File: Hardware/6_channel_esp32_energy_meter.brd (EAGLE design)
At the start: 61 x 62.2 mm, 117 parts, among them IC1 ATM90E32AS, IC2 ATM90E32AS, IC3 LMR14020SDDA, J16 PINHD-1X19, J4 9-12VAC, J5 PINHD1X1-SM1X01_SM, J6 PINHD1X1-SM1X01_SM, J8 PINHD1X1-SM1X01_SM, U1 ESP32-DEVKITC-32D, Y1 16.384MHz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

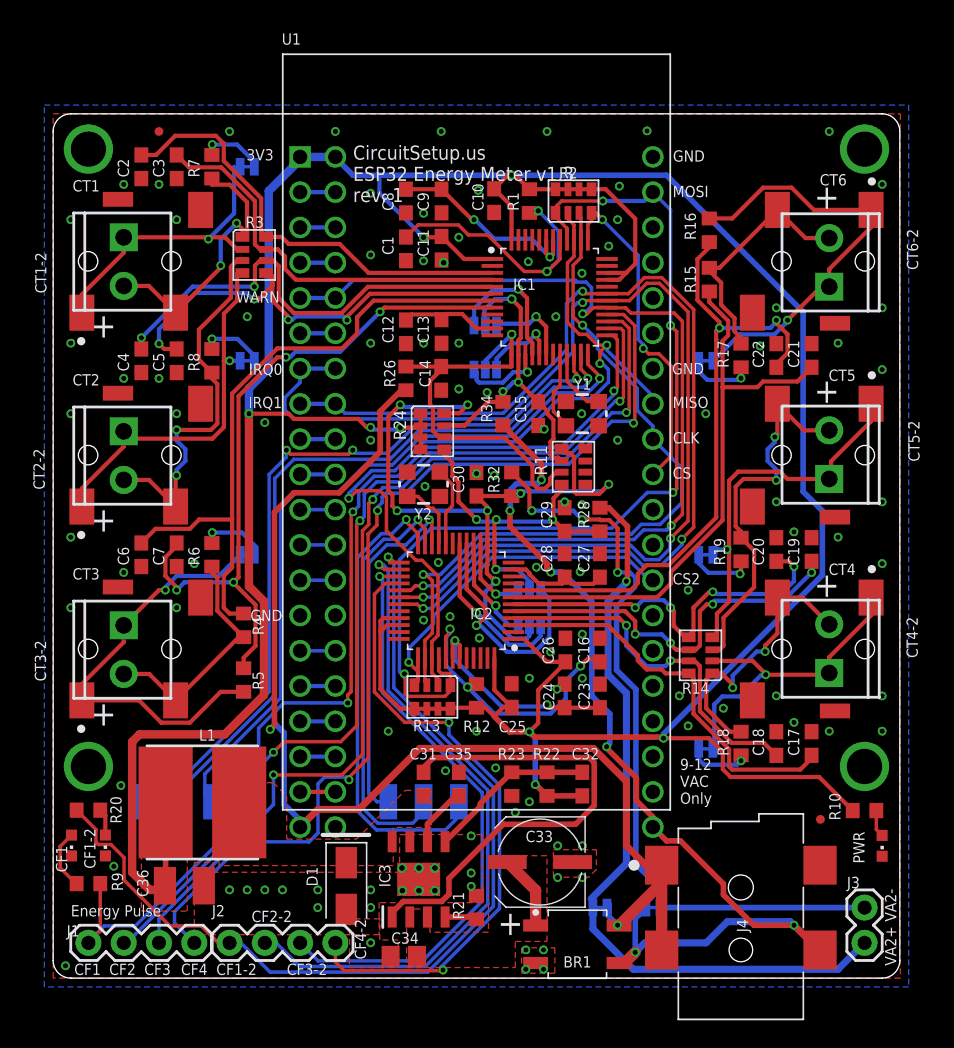
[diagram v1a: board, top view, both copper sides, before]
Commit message: v1.4
- Added optional micro-hdmi connection to connect the current transformer remote board. This allows for all 6 current transformer connections to connect to a remote pcb, which then connects to the main board via 1 micro-hdmi cable. Instead of 6 wires coming out of the meter, there can now be 1.
- Added current transformer remote pcb
- Removed JP8-JP11 and connected all voltage channels together for each ATM90E32
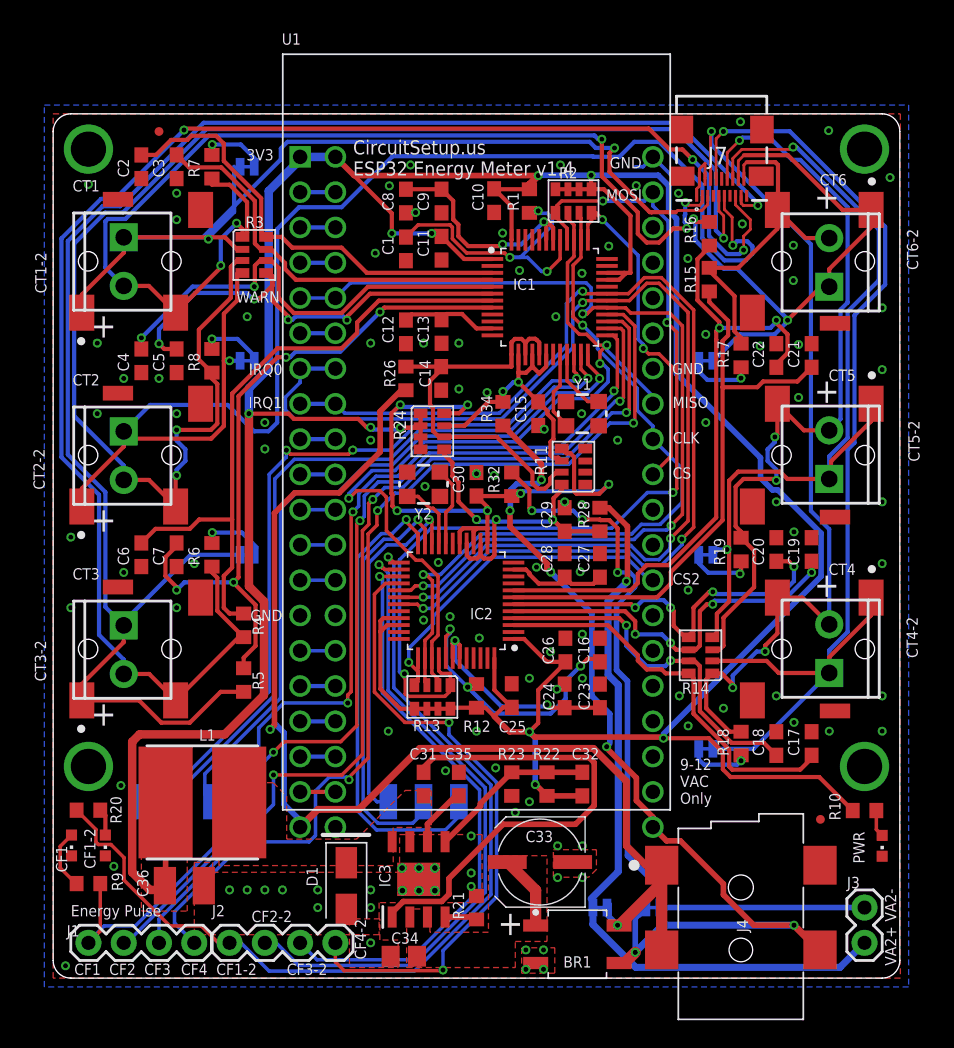
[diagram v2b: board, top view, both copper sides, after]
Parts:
- removed JP10, JP11, JP8, JP9: JUMPER-SMT_3_NO_SILK, SparkFun-Jumpers:SMT-JUMPER_3_NO_SILK
- added J7: 46765-0001, 46765-0001:46765-0001
- moved R16 0.25 mm to (47.2, 53.6)
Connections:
- removed net V2N: IC1.16, JP9.3
- removed net V2N-2: IC2.16, JP11.3
- removed net V2P: IC1.15, JP8.3
- removed net V2P-2: IC2.15, JP10.3
- removed net V3N: IC1.18, JP9.1
- removed net V3N-2: IC2.18, JP11.1
- removed net V3P: IC1.17, JP8.1
- removed net V3P-2: IC2.17, JP10.1
- net GND: now also J7.1, J7.10, J7.13, J7.2, J7.4, J7.7
- net IA+: now also J7.3
- net IA+-2: now also J7.6
- net IA-: now also J7.5
- net IA--2: now also J7.8
- net IB+: now also J7.9
- net IB+-2: now also J7.12
- net IB-: now also J7.11
- net IB--2: now also J7.14
- net IC+: now also J7.15
- net IC+-2: now also J7.18
- net IC-: now also J7.17
- net IC--2: now also J7.16
- net VAN: now also IC1.16, IC1.18; no longer JP9.2
- net VAN2: now also IC2.16, IC2.18; no longer JP11.2
- net VAP: now also IC1.15, IC1.17; no longer JP8.2
- net VAP2: now also IC2.15, IC2.17; no longer JP10.2
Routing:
- net IC+: track 17.3 -> 113.9 mm, vias 0 -> 3
- net IC-: track 30.5 -> 117.4 mm
- net IB+: track 27.5 -> 105.2 mm, vias 2 -> 3
- net IB-: track 27.6 -> 103.2 mm, vias 1 -> 2
- net IA+: track 20.1 -> 79.6 mm, vias 2 -> 5
- net IA--2: track 23.4 -> 78.0 mm
- net IA-: track 22.0 -> 71.8 mm, vias 1 -> 2
- net IA+-2: track 20.7 -> 63.1 mm, vias 2 -> 3
- net IB--2: track 27.5 -> 61.8 mm, vias 1 -> 2
- net IB+-2: track 27.7 -> 57.3 mm, vias 2 -> 3
- net V3P-2: track 17.0 -> 0.00 mm, vias 1 -> 0
- net V3N-2: track 12.1 -> 0.00 mm, vias 1 -> 0
- net IC--2: track 30.7 -> 41.4 mm, vias 1 -> 2
- net V2N: track 10.3 -> 0.00 mm, vias 1 -> 0
- net IC+-2: track 17.6 -> 25.3 mm
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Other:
- board text added: "CircuitSetup.us ESP32 Energy Meter v1.4"
- board text removed: "CircuitSetup.us ESP32 Energy Meter v1.3 rev. 1"
- board text removed: "JP8 - JP11: Connect the center pad with the 2 outer pads to connect all 3 voltage channels together for each IC"

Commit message: v1.4 rev1
- Changed micro-hdmi connector to through-hole
- Changed spacing on VA2+/VA2- (voltage 2 connection) to 3.5mm to allow for standard screw connectors
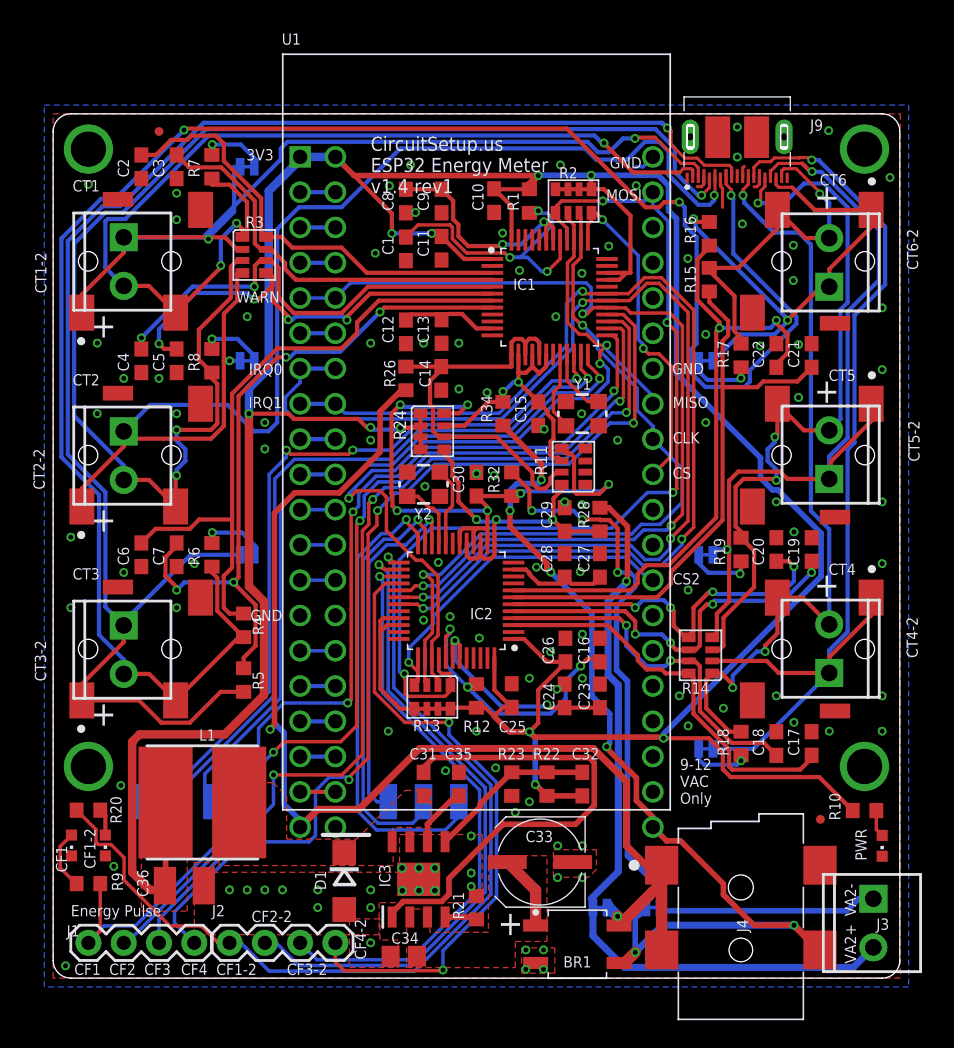
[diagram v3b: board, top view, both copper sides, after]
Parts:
- removed J7: 46765-0001, 46765-0001:46765-0001
- added J9: PKS019-4011-0, SamacSys_Parts:PKS01940110
- D1: value 500mV 3A -> (none); device SamacSys_Parts:DIOM4326X240 -> diode:DO214AC
- J3: device SparkFun-Connectors:1X02 -> SparkFun-Connectors:SCREWTERMINAL-3.5MM-2
- moved J3 3.24 mm to (59.1, 5.71), turned to 270 degrees
- moved D1 0.39 mm to (21.0, 6.99)
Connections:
- net GND: now also D1.A, J9.1, J9.10, J9.11, J9.14, J9.19, J9.21, J9.22, J9.4, J9.7, J9.P$1, J9.P$2; no longer D1.2, J7.1, J7.10, J7.13, J7.2, J7.4, J7.7
- net IA+: now also J9.2; no longer J7.3
- net IA+-2: now also J9.12; no longer J7.6
- net IA-: now also J9.3; no longer J7.5
- net IA--2: now also J9.13; no longer J7.8
- net IB+: now also J9.5; no longer J7.9
- net IB+-2: now also J9.15; no longer J7.12
- net IB-: now also J9.6; no longer J7.11
- net IB--2: now also J9.16; no longer J7.14
- net IC+: now also J9.8; no longer J7.15
- net IC+-2: now also J9.18; no longer J7.18
- net IC-: now also J9.9; no longer J7.17
- net IC--2: now also J9.17; no longer J7.16
- net SW: now also D1.C; no longer D1.1
- net VA2+: now also J3.2; no longer J3.1
- net VA2-: now also J3.1; no longer J3.2
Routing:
- net IC+: track 113.9 -> 137.4 mm
- net IB-: track 103.2 -> 93.9 mm
- net IA+: track 79.6 -> 71.8 mm, vias 5 -> 3
- net IA+-2: track 63.1 -> 56.6 mm
- net IB+: track 105.2 -> 99.1 mm
- net IA--2: track 78.0 -> 72.5 mm
- net IC--2: track 41.4 -> 36.1 mm
- net IB--2: track 61.8 -> 57.3 mm
- net IC-: track 117.4 -> 113.8 mm
- net IB+-2: track 57.3 -> 54.0 mm
- net IA-: track 71.8 -> 69.0 mm
- net VA+: track 88.7 -> 87.3 mm
- net VA2-: track 55.0 -> 56.1 mm
- net VA2+: track 54.0 -> 55.0 mm
- net IC+-2: track 25.3 -> 26.3 mm, vias 0 -> 1
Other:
- board text added: "CircuitSetup.us ESP32 Energy Meter v1.4 rev1"
- board text removed: "CircuitSetup.us ESP32 Energy Meter v1.4"

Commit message: Updated Eagle files to v1.4 rev1
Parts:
- C17, C18, C19, C2, C20, C21, C22, C3, C4, C5, C6, C7: value .33uF -> 18nf
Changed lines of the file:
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@@
 <?xml version="1.0" encoding="utf-8"?>
 <!DOCTYPE eagle SYSTEM "eagle.dtd">
-<eagle version="9.5.1">
+<eagle version="9.6.2">
 <drawing>
 <settings>
-<setting alwaysvectorfont="no"/>
+<setting alwaysvectorfont="yes"/>
 <setting keepoldvectorfont="yes"/>
 <setting verticaltext="up"/>
@@
 </layers>
 <board>
-<fusionsync huburn="a.cGVyc29uYWw6dWUyZGE1YzFh" projecturn="a.cGVyc29uYWw6dWUyZGE1YzFhIzIwMTgwODA3MTQyOTEzNDU2" f3durn="urn:adsk.wipprod:dm.lineage:77R0Z7BuTCq7n9YzdNgQcA" pcbguid="81154c38-d356-4f7c-b7d5-5c7aff837905" lastpulledtime="" lastsyncedchangeguid="6a4b892a-f070-e276-d825-ffa7404d0cf4"/>
+<fusionsync huburn="a.cGVyc29uYWw6dWUyZGE1YzFh" projecturn="a.cGVyc29uYWw6dWUyZGE1YzFhIzIwMTgwODA3MTQyOTEzNDU2" f3durn="urn:adsk.wipprod:dm.lineage:77R0Z7BuTCq7n9YzdNgQcA" pcbguid="81154c38-d356-4f7c-b7d5-5c7aff837905" lastpulledtime="" lastsyncedchangeguid="6a4b892a-f070-e276-d825-ffa7404d0cf4" latestrevisionid="" lastsyncedrevisionid="" lastboardhashguid="" lastpushedtime="" linktopcb3d="false"/>
 <plain>
 <text x="22.86" y="56.515" size="1.016" layer="25" font="vector" ratio="15">CircuitSetup.us
@@
 </autorouter>
 <elements>
-<element name="C2" library="rcl" library_urn="urn:adsk.eagle:library:334" package="C0603" package3d_urn="urn:adsk.eagle:package:23616/2" value=".33uF" x="6.35" y="58.42" smashed="yes" rot="R270">
+<element name="C2" library="rcl" library_urn="urn:adsk.eagle:library:334" package="C0603" package3d_urn="urn:adsk.eagle:package:23616/2" value="18nf" x="6.35" y="58.42" smashed="yes" rot="R270">
 <attribute name="NAME" x="5.461" y="57.658" size="0.8128" layer="25" font="vector" ratio="10" rot="R90"/>
 <attribute name="POPULARITY" value="37" x="6.35" y="58.42" size="1.778" layer="27" rot="R270" display="off"/>
@@
 <attribute name="VALUE" x="4.318" y="59.309" size="0.8" layer="27" rot="R270"/>
 </element>
-<element name="C3" library="rcl" library_urn="urn:adsk.eagle:library:334" package="C0603" package3d_urn="urn:adsk.eagle:package:23616/2" value=".33uF" x="8.89" y="58.42" smashed="yes" rot="R90">
+<element name="C3" library="rcl" library_urn="urn:adsk.eagle:library:334" package="C0603" package3d_urn="urn:adsk.eagle:package:23616/2" value="18nf" x="8.89" y="58.42" smashed="yes" rot="R90">
 <attribute name="NAME" x="8.001" y="57.658" size="0.8128" layer="25" font="vector" ratio="10" rot="R90"/>
 <attribute name="POPULARITY" value="37" x="8.89" y="58.42" size="1.778" layer="27" rot="R90" display="off"/>
@@
 <attribute name="VALUE" x="10.922" y="57.531" size="0.8" layer="27" rot="R90"/>
 </element>
-<element name="C4" library="rcl" library_urn="urn:adsk.eagle:library:334" package="C0603" package3d_urn="urn:adsk.eagle:package:23616/2" value=".33uF" x="6.35" y="44.45" smashed="yes" rot="R270">
+<element name="C4" library="rcl" library_urn="urn:adsk.eagle:library:334" package="C0603" package3d_urn="urn:adsk.eagle:package:23616/2" value="18nf" x="6.35" y="44.45" smashed="yes" rot="R270">
 <attribute name="NAME" x="5.461" y="43.688" size="0.8128" layer="25" font="vector" ratio="10" rot="R90"/>
 <attribute name="POPULARITY" value="37" x="6.35" y="44.45" size="1.778" layer="27" rot="R270" display="off"/>
@@
 <attribute name="VALUE" x="4.318" y="45.339" size="0.8" layer="27" rot="R270"/>
 </element>
-<element name="C5" library="rcl" library_urn="urn:adsk.eagle:library:334" package="C0603" package3d_urn="urn:adsk.eagle:package:23616/2" value=".33uF" x="8.89" y="44.45" smashed="yes" rot="R90">
+<element name="C5" library="rcl" library_urn="urn:adsk.eagle:library:334" package="C0603" package3d_urn="urn:adsk.eagle:package:23616/2" value="18nf" x="8.89" y="44.45" smashed="yes" rot="R90">
 <attribute name="NAME" x="8.001" y="43.688" size="0.8128" layer="25" font="vector" ratio="10" rot="R90"/>
 <attribute name="POPULARITY" value="37" x="8.89" y="44.45" size="1.778" layer="27" rot="R90" display="off"/>
@@
 <attribute name="VALUE" x="9.525" y="31.115" size="1.27" layer="27" rot="R270"/>
 </element>
-<element name="C6" library="rcl" library_urn="urn:adsk.eagle:library:334" package="C0603" package3d_urn="urn:adsk.eagle:package:23616/2" value=".33uF" x="6.35" y="30.48" smashed="yes" rot="R270">
+<element name="C6" library="rcl" library_urn="urn:adsk.eagle:library:334" package="C0603" package3d_urn="urn:adsk.eagle:package:23616/2" value="18nf" x="6.35" y="30.48" smashed="yes" rot="R270">
 <attribute name="NAME" x="5.461" y="29.718" size="0.8128" layer="25" font="vector" ratio="10" rot="R90"/>
 <attribute name="POPULARITY" value="37" x="6.35" y="30.48" size="1.778" layer="27" rot="R270" display="off"/>
@@
 <attribute name="VALUE" x="4.445" y="31.115" size="1.27" layer="27" rot="R270"/>
 </element>
-<element name="C7" library="rcl" library_urn="urn:adsk.eagle:library:334" package="C0603" package3d_urn="urn:adsk.eagle:package:23616/2" value=".33uF" x="8.89" y="30.48" smashed="yes" rot="R90">
+<element name="C7" library="rcl" library_urn="urn:adsk.eagle:library:334" package="C0603" package3d_urn="urn:adsk.eagle:package:23616/2" value="18nf" x="8.89" y="30.48" smashed="yes" rot="R90">
 <attribute name="NAME" x="8.001" y="29.718" size="0.8128" layer="25" font="vector" ratio="10" rot="R90"/>
 <attribute name="POPULARITY" value="37" x="8.89" y="30.48" size="1.778" layer="27" rot="R90" display="off"/>
@@
 <attribute name="VALUE" x="6.35" y="12.7" size="0.0254" layer="28" rot="MR0"/>
 </element>
-<element name="C17" library="rcl" library_urn="urn:adsk.eagle:library:334" package="C0603" package3d_urn="urn:adsk.eagle:package:23616/2" value=".33uF" x="54.61" y="16.891" smashed="yes" rot="R90">
+<element name="C17" library="rcl" library_urn="urn:adsk.eagle:library:334" package="C0603" package3d_urn="urn:adsk.eagle:package:23616/2" value="18nf" x="54.61" y="16.891" smashed="yes" rot="R90">
 <attribute name="NAME" x="53.721" y="16.002" size="0.8128" layer="25" font="vector" ratio="10" rot="R90"/>
 <attribute name="POPULARITY" value="37" x="54.61" y="16.891" size="1.778" layer="27" rot="R90" display="off"/>
@@
 <attribute name="VALUE" x="56.642" y="16.002" size="0.8" layer="27" rot="R90"/>
 </element>
-<element name="C18" library="rcl" library_urn="urn:adsk.eagle:library:334" package="C0603" package3d_urn="urn:adsk.eagle:package:23616/2" value=".33uF" x="52.07" y="16.891" smashed="yes" rot="R270">
+<element name="C18" library="rcl" library_urn="urn:adsk.eagle:library:334" package="C0603" package3d_urn="urn:adsk.eagle:package:23616/2" value="18nf" x="52.07" y="16.891" smashed="yes" rot="R270">
 <attribute name="NAME" x="51.181" y="16.002" size="0.8128" layer="25" font="vector" ratio="10" rot="R90"/>
 <attribute name="POPULARITY" value="37" x="52.07" y="16.891" size="1.778" layer="27" rot="R270" display="off"/>
@@
 <attribute name="VALUE" x="50.038" y="17.78" size="0.8" layer="27" rot="R270"/>
 </element>
-<element name="C19" library="rcl" library_urn="urn:adsk.eagle:library:334" package="C0603" package3d_urn="urn:adsk.eagle:package:23616/2" value=".33uF" x="54.61" y="30.861" smashed="yes" rot="R90">
+<element name="C19" library="rcl" library_urn="urn:adsk.eagle:library:334" package="C0603" package3d_urn="urn:adsk.eagle:package:23616/2" value="18nf" x="54.61" y="30.861" smashed="yes" rot="R90">
 <attribute name="NAME" x="53.721" y="29.718" size="0.8128" layer="25" font="vector" ratio="10" rot="R90"/>
 <attribute name="POPULARITY" value="37" x="54.61" y="30.861" size="1.778" layer="27" rot="R90" display="off"/>
@@
 <attribute name="VALUE" x="56.642" y="29.972" size="0.8" layer="27" rot="R90"/>
 </element>
-<element name="C20" library="rcl" library_urn="urn:adsk.eagle:library:334" package="C0603" package3d_urn="urn:adsk.eagle:package:23616/2" value=".33uF" x="52.07" y="30.861" smashed="yes" rot="R270">
+<element name="C20" library="rcl" library_urn="urn:adsk.eagle:library:334" package="C0603" package3d_urn="urn:adsk.eagle:package:23616/2" value="18nf" x="52.07" y="30.861" smashed="yes" rot="R270">
 <attribute name="NAME" x="51.181" y="29.718" size="0.8128" layer="25" font="vector" ratio="10" rot="R90"/>
 <attribute name="POPULARITY" value="37" x="52.07" y="30.861" size="1.778" layer="27" rot="R270" display="off"/>
@@
 <attribute name="VALUE" x="51.435" y="44.196" size="1.27" layer="27" rot="R90"/>
 </element>
-<element name="C21" library="rcl" library_urn="urn:adsk.eagle:library:334" package="C0603" package3d_urn="urn:adsk.eagle:package:23616/2" value=".33uF" x="54.61" y="44.831" smashed="yes" rot="R90">
+<element name="C21" library="rcl" library_urn="urn:adsk.eagle:library:334" package="C0603" package3d_urn="urn:adsk.eagle:package:23616/2" value="18nf" x="54.61" y="44.831" smashed="yes" rot="R90">
 <attribute name="NAME" x="53.721" y="43.942" size="0.8128" layer="25" font="vector" ratio="10" rot="R90"/>
 <attribute name="POPULARITY" value="37" x="54.61" y="44.831" size="1.778" layer="27" rot="R90" display="off"/>
@@
 <attribute name="VALUE" x="56.515" y="44.196" size="1.27" layer="27" rot="R90"/>
 </element>
-<element name="C22" library="rcl" library_urn="urn:adsk.eagle:library:334" package="C0603" package3d_urn="urn:adsk.eagle:package:23616/2" value=".33uF" x="52.07" y="44.831" smashed="yes" rot="R270">
+<element name="C22" library="rcl" library_urn="urn:adsk.eagle:library:334" package="C0603" package3d_urn="urn:adsk.eagle:package:23616/2" value="18nf" x="52.07" y="44.831" smashed="yes" rot="R270">
 <attribute name="NAME" x="51.181" y="43.942" size="0.8128" layer="25" font="vector" ratio="10" rot="R90"/>
 <attribute name="POPULARITY" value="37" x="52.07" y="44.831" size="1.778" layer="27" rot="R270" display="off"/>
